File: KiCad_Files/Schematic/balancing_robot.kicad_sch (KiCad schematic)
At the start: 15 parts, among them J1 USB_C_Receptacle_USB2.0, Q1 UMH3N, U1 ESP32-S3-WROOM-2, U2 CP2102N-Axx-xQFN28, U3 USBLC6-2P6

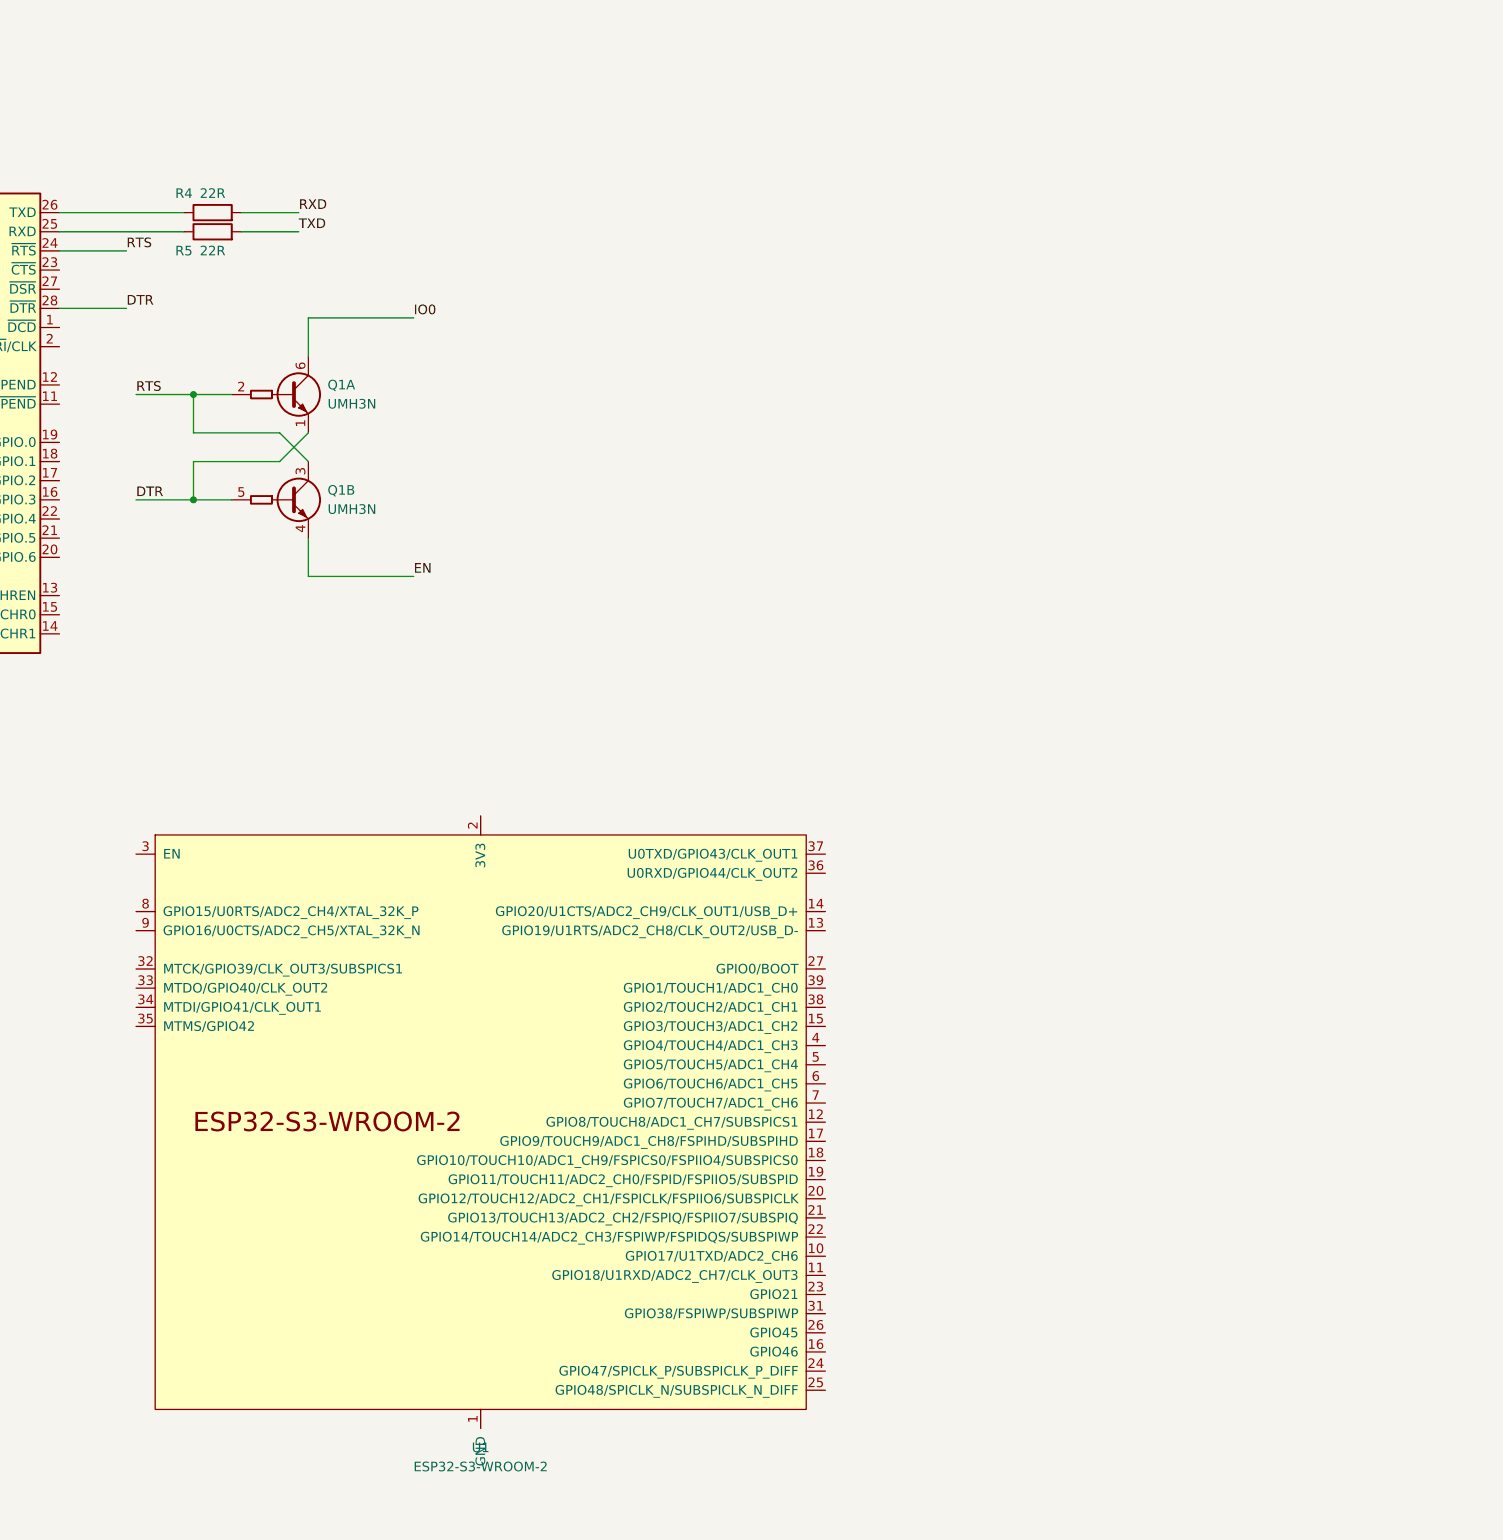
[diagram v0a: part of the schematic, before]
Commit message: Added BNO_0xx datasheet and schematic
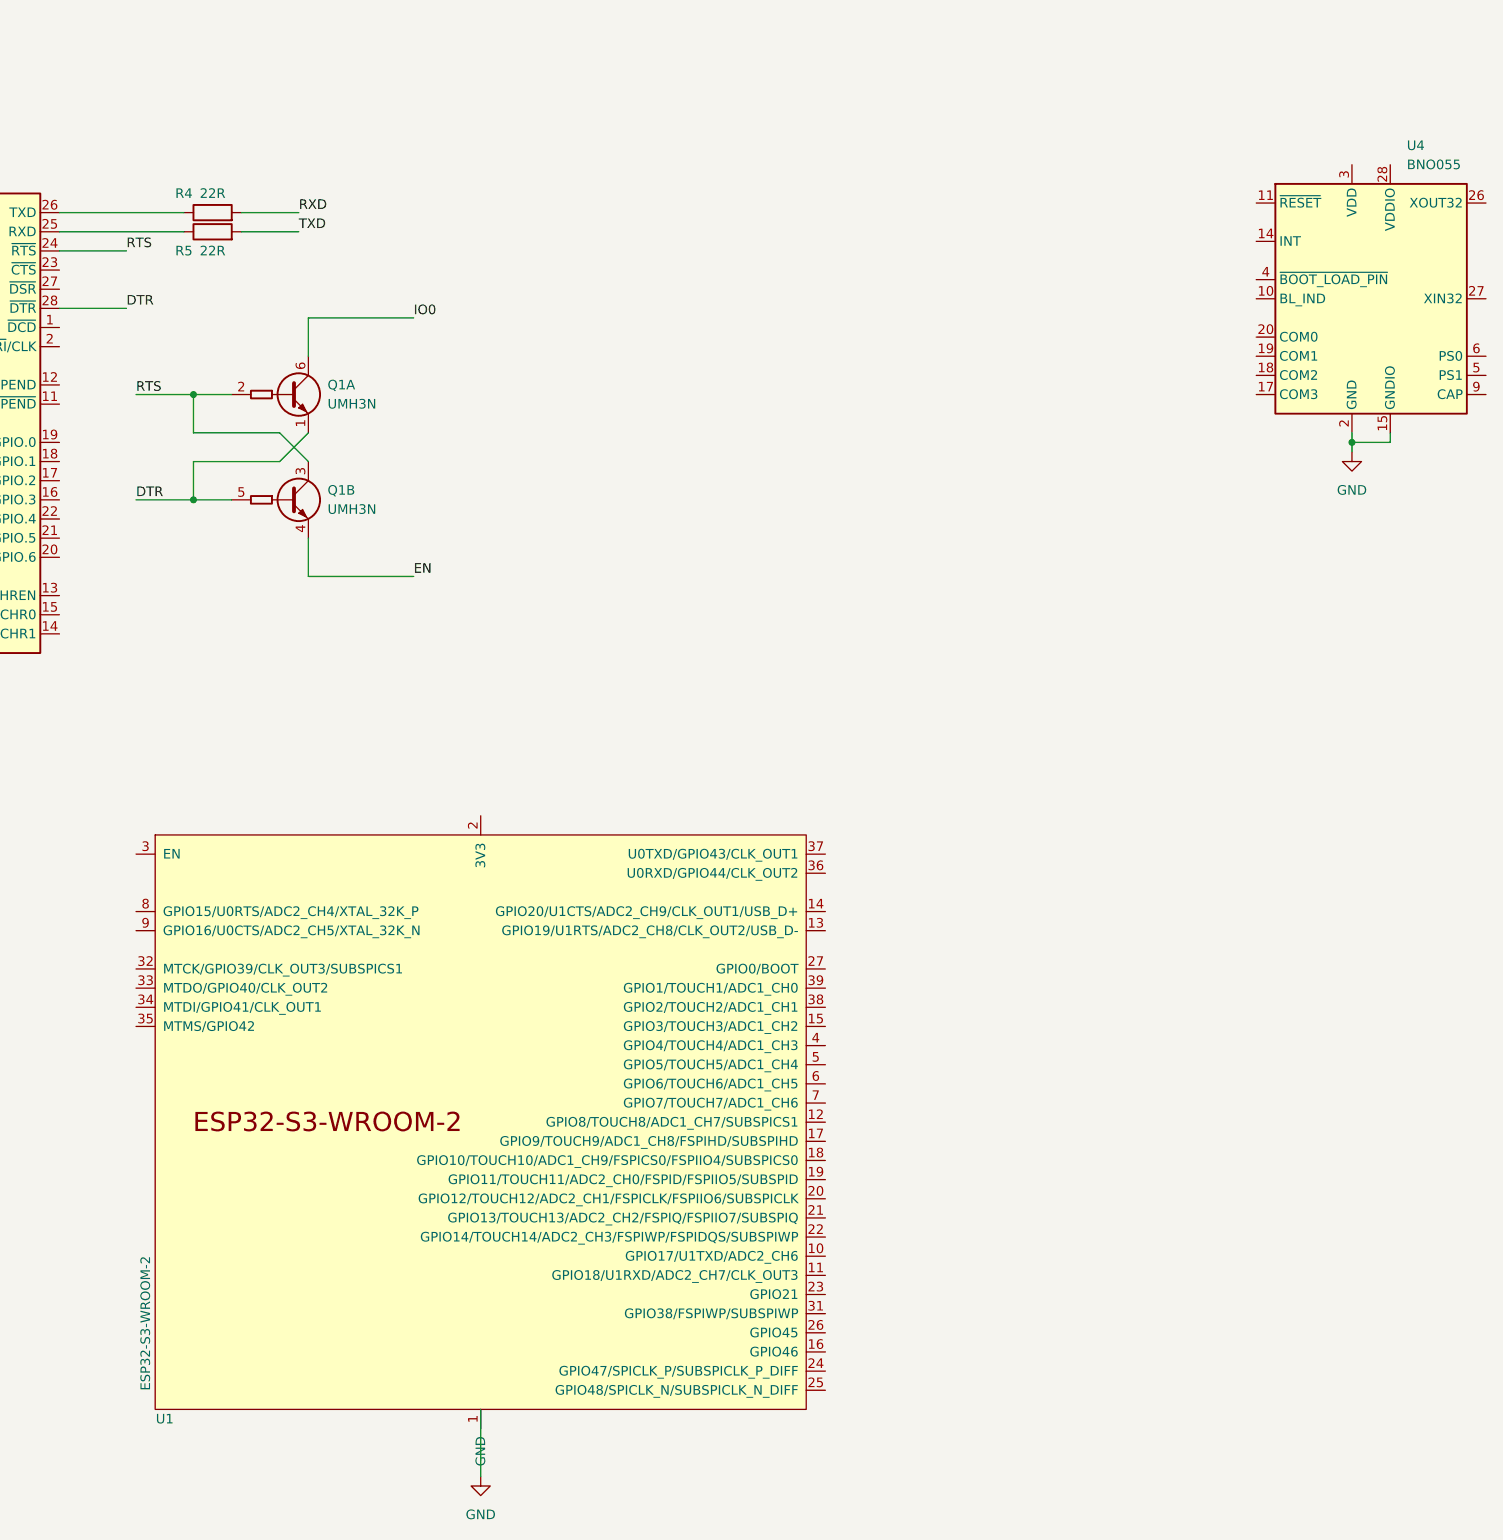
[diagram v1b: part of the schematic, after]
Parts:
- added U4: BNO055, Package_LGA:LGA-28_5.2x3.8mm_P0.5mm, symbol Sensor_Motion:BNO055
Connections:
- net GND: now also U1.1 (GND), U1.40 (GND), U1.41 (GND), U4.15 (GNDIO), U4.16 (GNDIO), U4.2 (GND), U4.25 (GNDIO)
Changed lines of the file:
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@@
   (junction (at 144.78 40.64) (diameter 0) (color 0 0 0 0)
   )
+  (junction (at 328.93 96.52) (diameter 0) (color 0 0 0 0)
+  )
   (junction (at 57.15 43.18) (diameter 0) (color 0 0 0 0)
   )
@@
     (stroke (width 0) (type default))
   )
+  (wire (pts (xy 334.01 95.25) (xy 334.01 96.52))
+    (stroke (width 0) (type default))
+  )
   (wire (pts (xy 97.79 43.18) (xy 109.22 43.18))
     (stroke (width 0) (type default))
@@
     (stroke (width 0) (type default))
   )
+  (wire (pts (xy 334.01 96.52) (xy 328.93 96.52))
+    (stroke (width 0) (type default))
+  )
   (wire (pts (xy 190.5 95.25) (xy 186.69 99.06))
     (stroke (width 0) (type default))
@@
     (stroke (width 0) (type default))
   )
+  (wire (pts (xy 328.93 95.25) (xy 328.93 96.52))
+    (stroke (width 0) (type default))
+  )
   (wire (pts (xy 68.58 95.25) (xy 68.58 101.6))
     (stroke (width 0) (type default))
@@
     (stroke (width 0) (type default))
   )
+  (wire (pts (xy 213.36 224.79) (xy 213.36 233.68))
+    (stroke (width 0) (type default))
+  )
   (wire (pts (xy 132.08 66.04) (xy 130.81 66.04))
     (stroke (width 0) (type default))
   )
   (wire (pts (xy 109.22 43.18) (xy 118.11 43.18))
+    (stroke (width 0) (type default))
+  )
+  (wire (pts (xy 328.93 96.52) (xy 328.93 97.79))
     (stroke (width 0) (type default))
   )
@@
     )
   )
+  (symbol (lib_id "power:GND") (at 213.36 233.68 0) (unit 1)
+    (in_bom yes) (on_board yes) (dnp no) (fields_autoplaced)
+    (property "Reference" "#PWR011" (at 213.36 240.03 0)
+      (effects (font (size 1.27 1.27)) hide)
+    )
+    (property "Value" "GND" (at 213.36 238.76 0)
+      (effects (font (size 1.27 1.27)))
+    )
+    (property "Footprint" "" (at 213.36 233.68 0)
+      (effects (font (size 1.27 1.27)) hide)
+    )
+    (property "Datasheet" "" (at 213.36 233.68 0)
+      (effects (font (size 1.27 1.27)) hide)
+    )
+    (pin "1")
+    (instances
+      (project "balancing_robot"
+        (path "/08a3ea21-c067-473b-9104-64f39401a454"
+          (reference "#PWR011") (unit 1)
+        )
+      )
+    )
+  )
   (symbol (lib_id "Device:R") (at 68.58 105.41 0) (unit 1)
     (in_bom yes) (on_board yes) (dnp no) (fields_autoplaced)
@@
     )
   )
+  (symbol (lib_id "Sensor_Motion:BNO055") (at 331.47 77.47 0) (unit 1)
+    (in_bom yes) (on_board yes) (dnp no) (fields_autoplaced)
+    (property "Reference" "U4" (at 336.2041 57.15 0)
+      (effects (font (size 1.27 1.27)) (justify left))
+    )
+    (property "Value" "BNO055" (at 336.2041 59.69 0)
+      (effects (font (size 1.27 1.27)) (justify left))
+    )
+    (property "Footprint" "Package_LGA:LGA-28_5.2x3.8mm_P0.5mm" (at 337.82 93.98 0)
+      (effects (font (size 1.27 1.27)) (justify left) hide)
+    )
+    (property "Datasheet" "https://www.bosch-sensortec.com/media/boschsensortec/downloads/datasheets/bst-bno055-ds000.pdf" (at 331.47 72.39 0)
+      (effects (font (size 1.27 1.27)) hide)
+    )
+    (pin "1")
+    (pin "10")
+    (pin "11")
+    (pin "12")
+    (pin "13")
+    (pin "14")
+    (pin "15")
+    (pin "16")
+    (pin "17")
+    (pin "18")
+    (pin "19")
+    (pin "2")
+    (pin "20")
+    (pin "21")
+    (pin "22")
+    (pin "23")
+    (pin "24")
+    (pin "25")
+    (pin "26")
+    (pin "27")
+    (pin "28")
+    (pin "3")
+    (pin "4")
+    (pin "5")
+    (pin "6")
+    (pin "7")
+    (pin "8")
+    (pin "9")
+    (instances
+      (project "balancing_robot"
+        (path "/08a3ea21-c067-473b-9104-64f39401a454"
+          (reference "U4") (unit 1)
+        )
+      )
+    )
+  )
   (symbol (lib_id "power:GND") (at 144.78 128.27 0) (unit 1)
     (in_bom yes) (on_board yes) (dnp no) (fields_autoplaced)
@@
   )
   (symbol (lib_id "PCM_Espressif:ESP32-S3-WROOM-2") (at 213.36 186.69 0) (unit 1)
-    (in_bom yes) (on_board yes) (dnp no) (fields_autoplaced)
-    (property "Reference" "U1" (at 213.36 229.87 0)
-      (effects (font (size 1.27 1.27)))
-    )
-    (property "Value" "ESP32-S3-WROOM-2" (at 213.36 232.41 0)
+    (in_bom yes) (on_board yes) (dnp no)
+    (property "Reference" "U1" (at 171.45 226.06 0)
+      (effects (font (size 1.27 1.27)))
+    )
+    (property "Value" "ESP32-S3-WROOM-2" (at 168.91 213.36 90)
       (effects (font (size 1.27 1.27)))
     )
@@
         )
       )
+    )
+  )
+  (symbol (lib_id "power:GND") (at 328.93 97.79 0) (unit 1)
+    (in_bom yes) (on_board yes) (dnp no) (fields_autoplaced)
+    (property "Reference" "#PWR010" (at 328.93 104.14 0)
+      (effects (font (size 1.27 1.27)) hide)
+    )
+    (property "Value" "GND" (at 328.93 102.87 0)
+      (effects (font (size 1.27 1.27)))
+    )
+    (property "Footprint" "" (at 328.93 97.79 0)
+      (effects (font (size 1.27 1.27)) hide)
+    )
+    (property "Datasheet" "" (at 328.93 97.79 0)
+      (effects (font (size 1.27 1.27)) hide)
+    )
+    (pin "1")
+    (instances
+      (project "balancing_robot"
+        (path "/08a3ea21-c067-473b-9104-64f39401a454"
+          (reference "#PWR010") (unit 1)
+        )
+      )

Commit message: Added Board Schematic and PCB and Code for MPU6050
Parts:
- removed F1: Polyfuse, symbol Device:Polyfuse
- removed U4: BNO055, Package_LGA:LGA-28_5.2x3.8mm_P0.5mm, symbol Sensor_Motion:BNO055
- added C1: 1u, Capacitor_THT:CP_Radial_D5.0mm_P2.50mm, symbol Device:C_Polarized
- added C10, C11, C2, C5: 22u, Capacitor_SMD:C_1206_3216Metric, symbol Device:C
- added C12: 75p, Capacitor_SMD:C_1206_3216Metric, symbol Device:C
- added C13, C15: 100n, Capacitor_THT:C_Disc_D5.0mm_W2.5mm_P5.00mm, symbol Device:C
- added C14: 22u, Capacitor_THT:C_Disc_D5.0mm_W2.5mm_P5.00mm, symbol Device:C
- added C3: 10u, Capacitor_THT:CP_Radial_D5.0mm_P2.50mm, symbol Device:C_Polarized
- added C4, C8: 0.1u, Capacitor_SMD:C_1206_3216Metric, symbol Device:C
- added D1: RED, LED_THT:LED_D3.0mm, symbol Device:LED
- added D2: 1N5819, Diode_THT:D_DO-41_SOD81_P10.16mm_Horizontal, symbol Diode:1N5819
- added D3: GREEN, LED_THT:LED_D3.0mm, symbol Device:LED
- added H1, H2, H3, H4: Hole_Pad, MountingHole:MountingHole_3.2mm_M3_Pad_Via, symbol Mechanical:MountingHole_Pad
- added J1: Screw_Terminal_01x02, TerminalBlock_Phoenix:TerminalBlock_Phoenix_MKDS-1,5-2-5.08_1x02_P5.08mm_Horizontal, symbol Connector:Screw_Terminal_01x02
- added J3, J4, J5, J6, J7, J8, J9: Conn_01x05, Connector_JST:JST_XH_B5B-XH-AM_1x05_P2.50mm_Vertical, symbol Connector_Generic:Conn_01x05
- added L1: 10u, Inductor_SMD:L_Bourns_SRP1245A, symbol Device:L
- added R1, R6: 1K, Resistor_THT:R_Axial_DIN0207_L6.3mm_D2.5mm_P10.16mm_Horizontal, symbol Device:R_Small
- added R11: 49.9, Resistor_SMD:R_1206_3216Metric, symbol Device:R
- added R12: 100k, Resistor_SMD:R_1206_3216Metric, symbol Device:R
- added R13: 13k3, Resistor_SMD:R_1206_3216Metric, symbol Device:R
- added R14, R7: 3k3, Resistor_THT:R_Axial_DIN0207_L6.3mm_D2.5mm_P10.16mm_Horizontal, symbol Device:R_Small
- added R15: 10k, Resistor_SMD:R_1206_3216Metric, symbol Device:R_Small
- added R4: 511k, Resistor_SMD:R_1206_3216Metric, symbol Device:R
- added R5: 105k, Resistor_SMD:R_1206_3216Metric, symbol Device:R
- added U1: TLV1117LV-3.3, Package_TO_SOT_SMD:SOT-223-3_TabPin2, symbol Regulator_Linear:LM1117MP-3.3
- added U3: TPS54302, Package_TO_SOT_SMD:SOT-23-6, symbol Regulator_Switching:TPS54302
- C9: renamed from C3; footprint Capacitor_THT:C_Disc_D5.0mm_W2.5mm_P5.00mm -> Capacitor_SMD:C_1206_3216Metric
- FB1: footprint (none) -> Inductor_SMD:L_0603_1608Metric
- R2: renamed from R1; footprint Resistor_THT:R_Axial_DIN0207_L6.3mm_D2.5mm_P10.16mm_Horizontal -> Resistor_SMD:R_1206_3216Metric
- R3: renamed from R2; footprint Resistor_THT:R_Axial_DIN0207_L6.3mm_D2.5mm_P10.16mm_Horizontal -> Resistor_SMD:R_1206_3216Metric
- R8: renamed from R3; footprint Resistor_THT:R_Axial_DIN0207_L6.3mm_D2.5mm_P10.16mm_Horizontal -> Resistor_SMD:R_1206_3216Metric
- renumbered C1 to C6, C2 to C7, J1 to J2, R5 to R10, R4 to R9, U3 to U2, U2 to U4, U1 to U5
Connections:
- net +5V: now also FB1.2, U2.2 (GND), C2.1, R1.1, U1.3 (VI)
- net +5VP: now also C10.1, C11.1, D2.1 (K), L1.2, R11.1; no longer J2.A4 (VBUS), J2.A9 (VBUS), J2.B4 (VBUS), J2.B9 (VBUS)
- net EN: now also Q1.3 (C2), U5.3 (EN), C13.1, R15.2; no longer Q1.4 (E2)
- net GND: now also J2.A1 (GND), J2.A12 (GND), J2.B1 (GND), J2.B12 (GND), J2.S1 (SHIELD), U2.5 (VBUS), C1.2, C10.2, C11.2, C13.2, C14.2, C15.2, C2.2, C3.2, C4.2, C5.2, D1.1 (K), D3.1 (K), H1.1, H2.1, H3.1, H4.1, J1.1 (Pin_1), J3.5 (Pin_5), J4.5 (Pin_5), J5.5 (Pin_5), J6.5 (Pin_5), J7.5 (Pin_5), J8.5 (Pin_5), J9.5 (Pin_5), R13.2, R5.2, U1.1 (GND), U3.1 (GND); no longer U2.2 (GND)
- net IO0: now also U5.27 (GPIO0/BOOT)
- net RTS: now also Q1.4 (E2); no longer Q1.3 (C2)
- net RXD: now also U5.36 (U0RXD/GPIO44/CLK_OUT2)
- net TXD: now also U5.37 (U0TXD/GPIO43/CLK_OUT1)
- net at J2.A6 (D+), J2.B6 (D+): now also U2.6 (I/O1); no longer U2.1 (I/O1)
- net at J2.A7 (D-), J2.B7 (D-): now also U2.4 (I/O2); no longer U2.3 (I/O2)
- net SDA: now reaches U5.12 (GPIO8/TOUCH8/ADC1_CH7/SUBSPICS1)
- net SDA: now also J3.2 (Pin_2), J4.2 (Pin_2), J5.2 (Pin_2), J6.2 (Pin_2), J7.2 (Pin_2), R7.2
- net SCL: now reaches U5.17 (GPIO9/TOUCH9/ADC1_CH8/FSPIHD/SUBSPIHD)
- net SCL: now also J3.3 (Pin_3), J4.3 (Pin_3), J5.3 (Pin_3), J6.3 (Pin_3), J7.3 (Pin_3), R14.2
- net +3.3V: now reaches U5.2 (3V3)
- net +3.3V: now also C14.1, C15.1, C5.1, J3.1 (Pin_1), J4.1 (Pin_1), J5.1 (Pin_1), J6.1 (Pin_1), J7.1 (Pin_1), R14.1, R15.1, R6.1, R7.1, U1.2 (VO)
- net RES_1: now reaches U5.20 (GPIO12/TOUCH12/ADC2_CH1/FSPICLK/FSPIIO6/SUBSPICLK)
- net RES_1: now also J3.4 (Pin_4)
- net RES_2: now reaches U5.21 (GPIO13/TOUCH13/ADC2_CH2/FSPIQ/FSPIIO7/SUBSPIQ)
- net RES_2: now also J5.4 (Pin_4)
- net RES_3: now reaches U5.22 (GPIO14/TOUCH14/ADC2_CH3/FSPIWP/FSPIDQS/SUBSPIWP)
- net RES_3: now also J7.4 (Pin_4)
- net MPU6050: now reaches U5.24 (GPIO47/SPICLK_P/SUBSPICLK_P_DIFF)
- net MPU6050: now also J4.4 (Pin_4)
- net VL53L0X: now reaches U5.25 (GPIO48/SPICLK_N/SUBSPICLK_N_DIFF)
- net VL53L0X: now also J6.4 (Pin_4)
- net PWM_A: now reaches U5.4 (GPIO4/TOUCH4/ADC1_CH3)
- net PWM_A: now also J8.2 (Pin_2)
- net A1: now reaches U5.5 (GPIO5/TOUCH5/ADC1_CH4)
- net A1: now also J8.3 (Pin_3)
- net A2: now reaches U5.6 (GPIO6/TOUCH6/ADC1_CH5)
- net A2: now also J8.4 (Pin_4)
- net PWM_B: now reaches U5.7 (GPIO7/TOUCH7/ADC1_CH6)
- net PWM_B: now also J9.2 (Pin_2)
- net B1: now reaches U5.8 (GPIO15/U0RTS/ADC2_CH4/XTAL_32K_P)
- net B1: now also J9.3 (Pin_3)
- net B2: now reaches U5.9 (GPIO16/U0CTS/ADC2_CH5/XTAL_32K_N)
- net B2: now also J9.4 (Pin_4)
- net at U4.5 (D-): now also U2.3 (I/O2); no longer U2.4 (I/O2)
- net at U4.4 (D+): now also U2.1 (I/O1); no longer U2.6 (I/O1)
- new net: C8.2, L1.1, U3.2 (SW)
- new net: C12.2, R12.2, R13.1, U3.4 (FB)
- new net: R4.2, R5.1, U3.5 (EN)
- new net: C8.1, U3.6 (BOOT)
- new net: C12.1, R11.2, R12.1
- new net: D2.2 (A), J2.A4 (VBUS), J2.A9 (VBUS), J2.B4 (VBUS), J2.B9 (VBUS)
- new net: D3.2 (A), R6.2
- new net: D1.2 (A), R1.2
- new net +12VA: C1.1, C3.1, C4.1, J1.2 (Pin_2), J8.1 (Pin_1), J9.1 (Pin_1), R4.1, U3.3 (VIN)
- no-connect marks 0 -> 35
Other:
- note added: "12V-5V BUCK CONVERTER"
- note added: "5V-3.3V LDO"
- note added: "GY-521 MPU6050"
- note added: "I2C BUS"
- note added: "MCU"
- note added: "MOTOR CONTROL"
- note added: "MOUNTING"
- note added: "PROGRAMMING INTERFACE"
- note added: "Reserve"
- note added: "VL53L0X"
- note removed: "POWER + PROGRAMMING INTERFACE"
- moved on the sheet: FB1, U2, U5
